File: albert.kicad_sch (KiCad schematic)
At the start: 0 parts

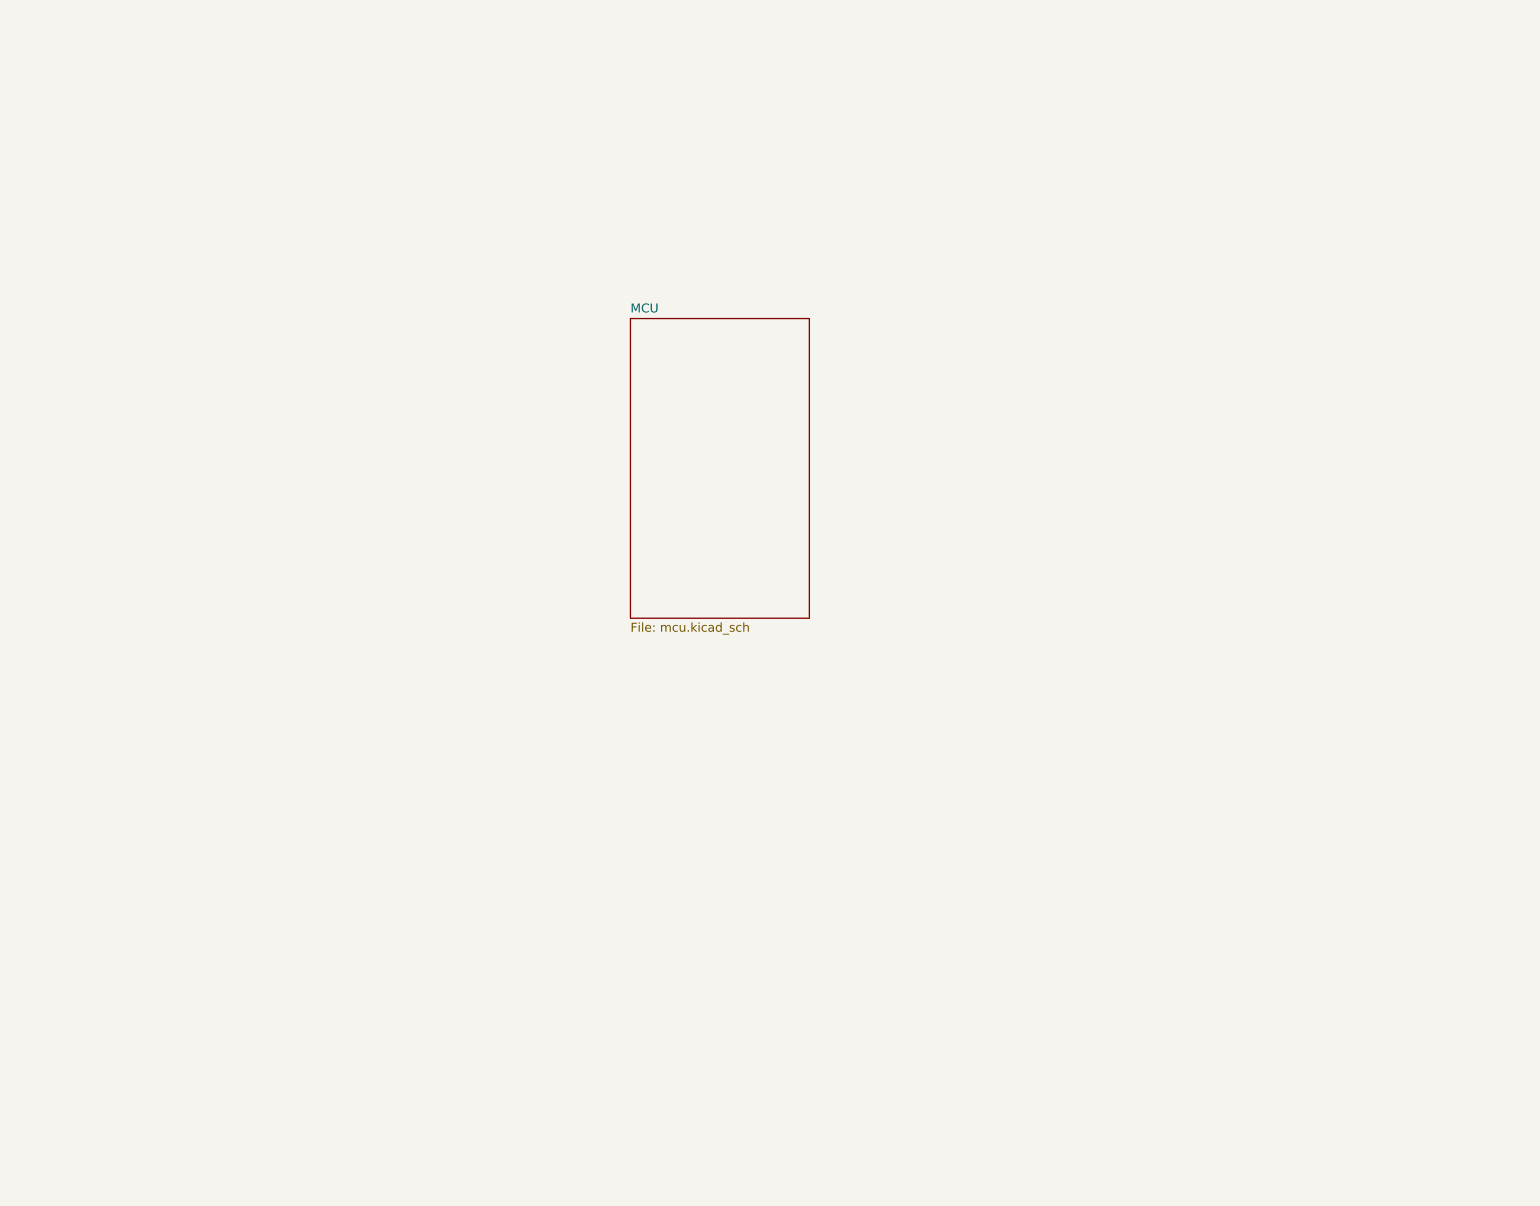
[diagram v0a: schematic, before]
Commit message: Finished XMOS schematic, began work on board connectors
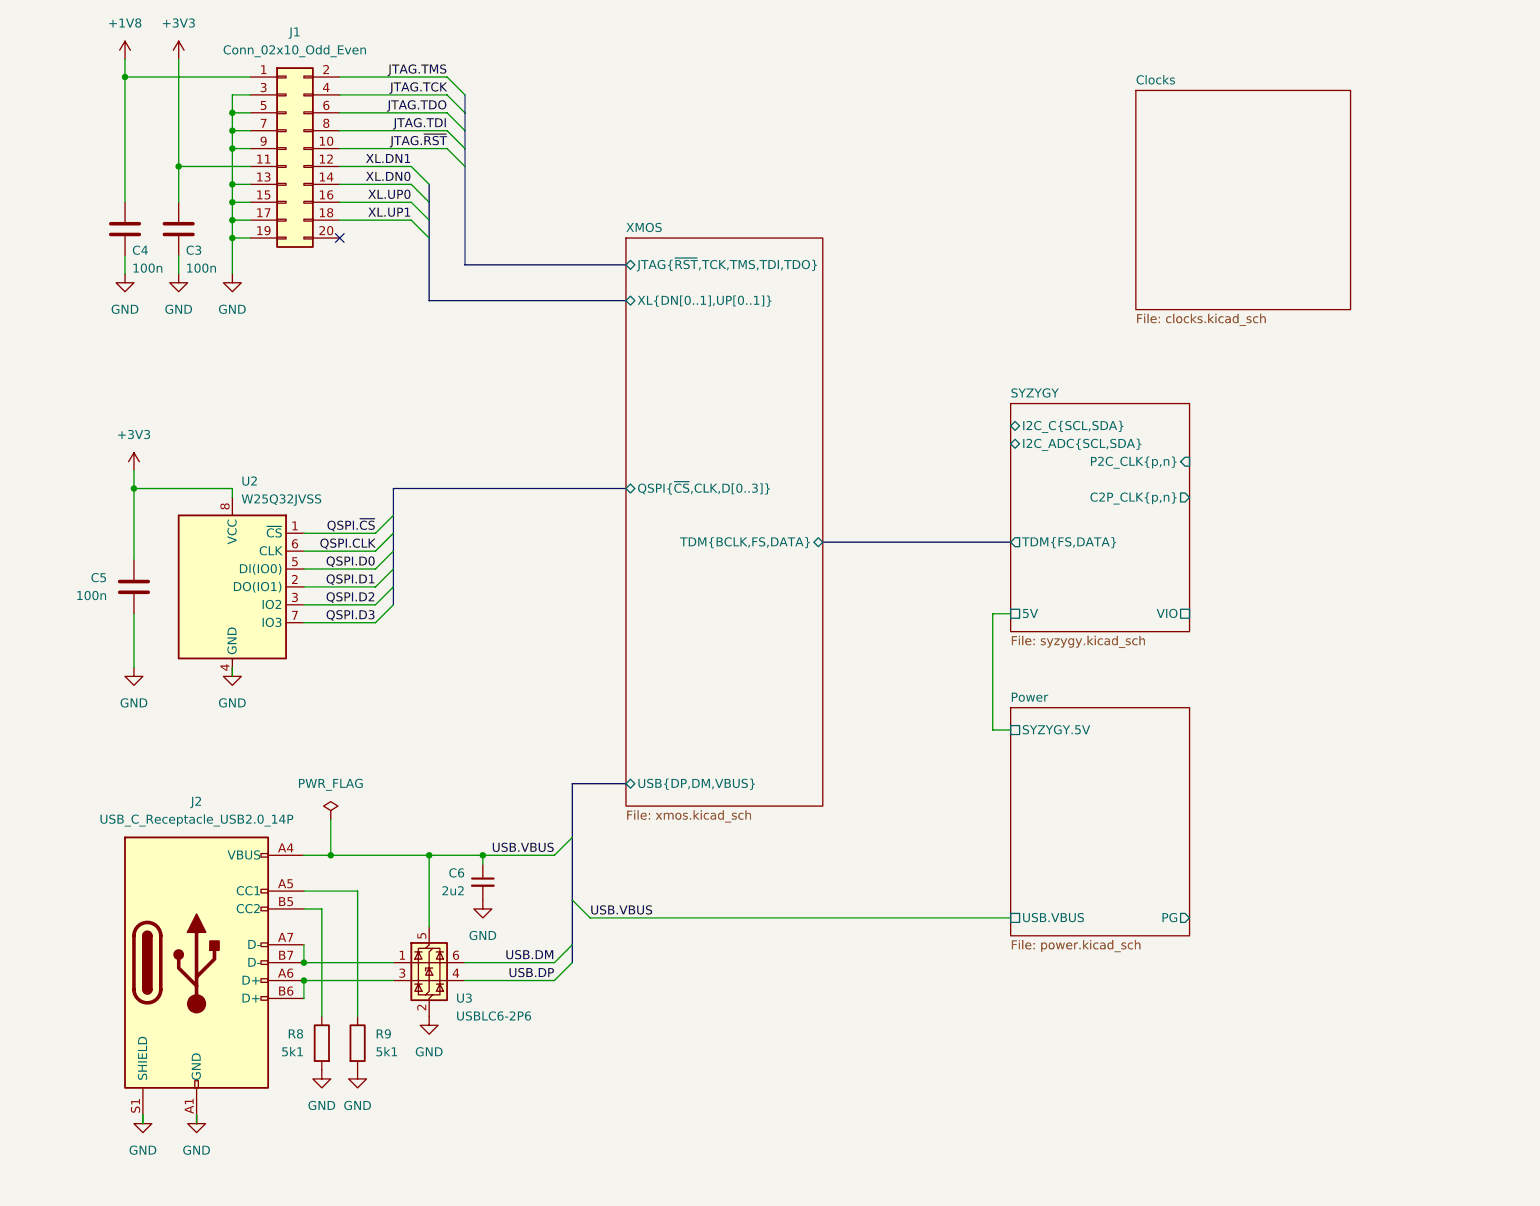
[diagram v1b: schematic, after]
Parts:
- added C3, C4, C5: 100n, symbol Device:C
- added C6: 2u2, symbol Device:C_Small
- added J1: Conn_02x10_Odd_Even, symbol Connector_Generic:Conn_02x10_Odd_Even
- added J2: USB_C_Receptacle_USB2.0_14P, symbol Connector:USB_C_Receptacle_USB2.0_14P
- added R8, R9: 5k1, symbol Device:R
- added U2: W25Q32JVSS, Package_SO:SOIC-8_5.23x5.23mm_P1.27mm, symbol Memory_Flash:W25Q32JVSS
- added U3: USBLC6-2P6, Package_TO_SOT_SMD:SOT-666, symbol Power_Protection:USBLC6-2P6
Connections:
- new net: J2.A7 (D-), J2.B7 (D-), U3.1 (I/O1)
- new net: J2.A6 (D+), J2.B6 (D+), U3.3 (I/O2)
- new net: J2.B5 (CC2), R8.1
- new net: J2.A5 (CC1), R9.1
- new net +1V8: C4.1, J1.1 (Pin_1)
- new net +3V3: C3.1, C5.1, J1.11 (Pin_11), U2.8 (VCC)
- new net GND: C3.2, C4.2, C5.2, C6.2, J1.13 (Pin_13), J1.15 (Pin_15), J1.17 (Pin_17), J1.19 (Pin_19), J1.3 (Pin_3), J1.5 (Pin_5), J1.7 (Pin_7), J1.9 (Pin_9), J2.A1 (GND), J2.A12 (GND), J2.B1 (GND), J2.B12 (GND), J2.S1 (SHIELD), R8.2, R9.2, U2.4 (GND), U3.2 (GND)
- new net JTAG.TCK: J1.4 (Pin_4)
- new net JTAG.TDI: J1.8 (Pin_8)
- new net JTAG.TDO: J1.6 (Pin_6)
- new net JTAG.TMS: J1.2 (Pin_2)
- new net JTAG.~{RST}: J1.10 (Pin_10)
- new net QSPI.CLK: U2.6 (CLK)
- new net QSPI.D0: U2.5 (DI(IO0))
- new net QSPI.D1: U2.2 (DO(IO1))
- new net QSPI.D2: U2.3 (IO2)
- new net QSPI.D3: U2.7 (IO3)
- new net QSPI.~{CS}: U2.1 (~{CS})
- new net USB.DM: U3.6 (I/O1)
- new net USB.DP: U3.4 (I/O2)
- new net USB.VBUS: C6.1, J2.A4 (VBUS), J2.A9 (VBUS), J2.B4 (VBUS), J2.B9 (VBUS), U3.5 (VBUS)
- new net XL.DN0: J1.14 (Pin_14)
- new net XL.DN1: J1.12 (Pin_12)
- new net XL.UP0: J1.16 (Pin_16)
- new net XL.UP1: J1.18 (Pin_18)
- no-connect marks 0 -> 1
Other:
- sheet MCU renamed XMOS
- added sheet Clocks (clocks.kicad_sch)
- added sheet Power (power.kicad_sch)
- added sheet SYZYGY (syzygy.kicad_sch)
- sheet XMOS: file mcu.kicad_sch -> xmos.kicad_sch
- sheet XMOS ports: added JTAG{~{RST},TCK,TMS,TDI,TDO}, QSPI{~{CS},CLK,D[0..3]}, TDM{BCLK,FS,DATA}, USB{DP,DM,VBUS}, XL{DN[0..1],UP[0..1]}; removed none

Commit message: Converted connector power to global labels
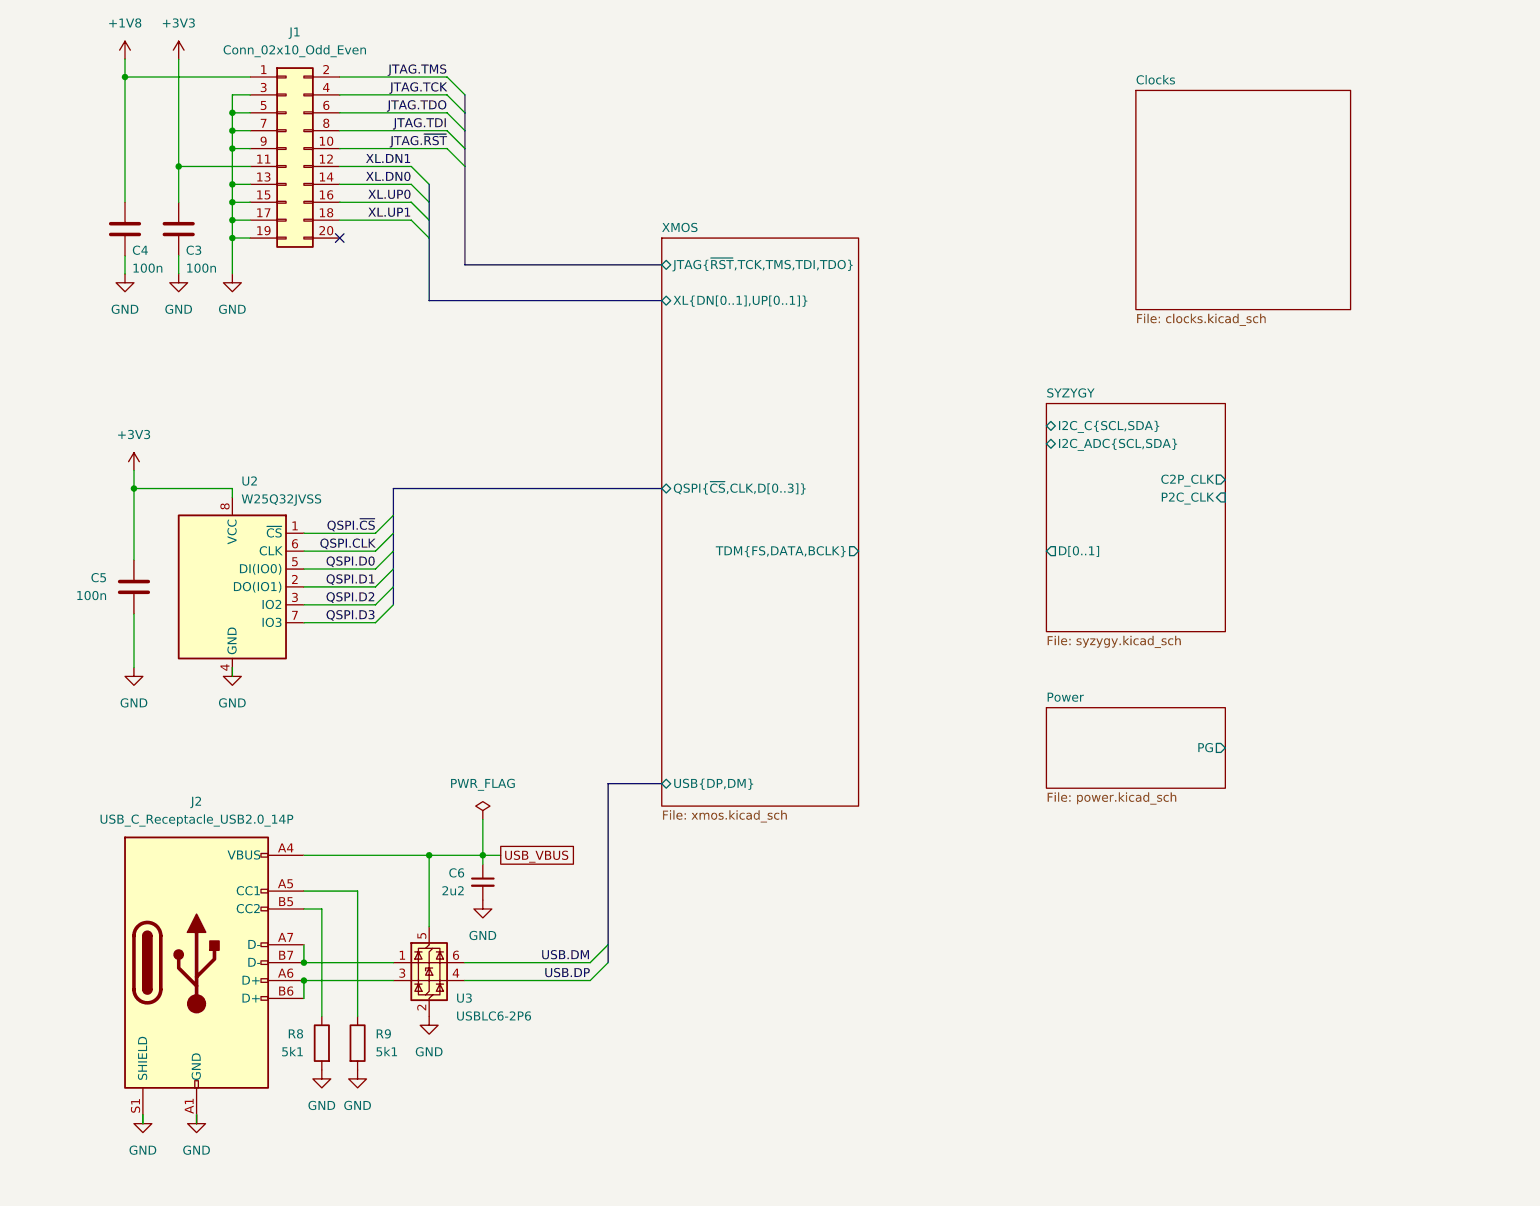
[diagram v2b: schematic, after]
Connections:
- net USB.VBUS renamed USB_VBUS
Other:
- sheet Power ports: added none; removed SYZYGY.5V, USB.VBUS
- sheet SYZYGY ports: added C2P_CLK, D[0..1], P2C_CLK; removed 5V, C2P_CLK{p,n}, P2C_CLK{p,n}, TDM{FS,DATA}, VIO
- sheet XMOS ports: added TDM{FS,DATA,BCLK}, USB{DP,DM}; removed TDM{BCLK,FS,DATA}, USB{DP,DM,VBUS}

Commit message: Minor updates
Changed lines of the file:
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@@
+	)
+	(bus_entry
+		(at 151.13 95.25)
+		(size 2.54 2.54)
+		(stroke
+			(width 0)
+			(type default)
+		)
 	)
 	(bus_entry
@@
 	)
 	(bus_entry
+		(at 148.59 76.2)
+		(size 2.54 2.54)
+		(stroke
+			(width 0)
+			(type default)
+		)
+	)
+	(bus_entry
+		(at 148.59 76.2)
+		(size 2.54 -2.54)
+		(stroke
+			(width 0)
+			(type default)
+		)
+	)
+	(bus_entry
 		(at 74.93 50.8)
+		(size 2.54 2.54)
+		(stroke
+			(width 0)
+			(type default)
+		)
+	)
+	(bus_entry
+		(at 148.59 95.25)
 		(size 2.54 2.54)
 		(stroke
@@
 	)
 	(bus_entry
+		(at 146.05 76.2)
+		(size 2.54 2.54)
+		(stroke
+			(width 0)
+			(type default)
+		)
+	)
+	(bus_entry
 		(at 69.85 97.79)
 		(size 2.54 -2.54)
@@
 		)
 	)
+	(bus
+		(pts
+			(xy 153.67 97.79) (xy 165.1 97.79)
+		)
+		(stroke
+			(width 0)
+			(type default)
+		)
+	)
 	(wire
 		(pts
@@
 		)
 	)
+	(bus
+		(pts
+			(xy 151.13 97.79) (xy 153.67 97.79)
+		)
+		(stroke
+			(width 0)
+			(type default)
+		)
+	)
+	(bus
+		(pts
+			(xy 138.43 76.2) (xy 146.05 76.2)
+		)
+		(stroke
+			(width 0)
+			(type default)
+		)
+	)
+	(bus
+		(pts
+			(xy 146.05 76.2) (xy 148.59 76.2)
+		)
+		(stroke
+			(width 0)
+			(type default)
+		)
+	)
+	(wire
+		(pts
+			(xy 148.59 78.74) (xy 148.59 95.25)
+		)
+		(stroke
+			(width 0)
+			(type default)
+		)
+	)
 	(wire
 		(pts
@@
 		)
 	)
+	(wire
+		(pts
+			(xy 151.13 78.74) (xy 151.13 95.25)
+		)
+		(stroke
+			(width 0)
+			(type default)
+		)
+	)
 	(bus
 		(pts
@@
 		(pts
 			(xy 49.53 115.57) (xy 49.53 114.3)
+		)
+		(stroke
+			(width 0)
+			(type default)
+		)
+	)
+	(wire
+		(pts
+			(xy 151.13 63.5) (xy 151.13 73.66)
 		)
 		(stroke
@@
 		)
 	)
-	(label "QSPI.D2"
-		(at 69.85 105.41 180)
+	(label "D1"
+		(at 148.59 95.25 90)
 		(fields_autoplaced yes)
 		(effects
@@
 				(size 1.27 1.27)
 			)
-			(justify right bottom)
-		)
-	)
-	(label "JTAG.TCK"
-		(at 80.01 33.02 180)
+			(justify left bottom)
+		)
+	)
+	(label "TDM.DATA"
+		(at 151.13 78.74 270)
 		(fields_autoplaced yes)
 		(effects
@@
 		)
 	)
-	(label "XL.UP1"
-		(at 74.93 50.8 180)
+	(label "QSPI.D2"
+		(at 69.85 105.41 180)
 		(fields_autoplaced yes)
 		(effects
@@
 		)
 	)
-	(label "QSPI.~{CS}"
-		(at 69.85 95.25 180)
+	(label "JTAG.TCK"
+		(at 80.01 33.02 180)
 		(fields_autoplaced yes)
 		(effects
@@
 		)
 	)
-	(label "USB.DM"
-		(at 100.33 156.21 180)
+	(label "XL.UP1"
+		(at 74.93 50.8 180)
 		(fields_autoplaced yes)
 		(effects
@@
 		)
 	)
-	(label "QSPI.D3"
-		(at 69.85 107.95 180)
+	(label "QSPI.~{CS}"
+		(at 69.85 95.25 180)
 		(fields_autoplaced yes)
 		(effects
@@
 		)
 	)
-	(label "QSPI.CLK"
-		(at 69.85 97.79 180)
+	(label "USB.DM"
+		(at 100.33 156.21 180)
 		(fields_autoplaced yes)
 		(effects
@@
 		)
 	)
-	(label "JTAG.TMS"
-		(at 80.01 30.48 180)
+	(label "QSPI.D3"
+		(at 69.85 107.95 180)
 		(fields_autoplaced yes)
 		(effects
@@
 		)
 	)
-	(label "JTAG.TDI"
-		(at 80.01 38.1 180)
+	(label "TDM.FS"
+		(at 148.59 78.74 270)
 		(fields_autoplaced yes)
 		(effects
@@
 		)
 	)
-	(label "JTAG.~{RST}"
-		(at 80.01 40.64 180)
+	(label "QSPI.CLK"
+		(at 69.85 97.79 180)
 		(fields_autoplaced yes)
 		(effects
@@
 		)
 	)
-	(label "USB.DP"
-		(at 100.33 158.75 180)
+	(label "JTAG.TMS"
+		(at 80.01 30.48 180)
 		(fields_autoplaced yes)
 		(effects
@@
 			)
 			(justify right bottom)
+		)
+	)
+	(label "D0"
+		(at 151.13 95.25 90)
+		(fields_autoplaced yes)
+		(effects
+			(font
+				(size 1.27 1.27)
+			)
+			(justify left bottom)
+		)
+	)
+	(label "JTAG.TDI"
+		(at 80.01 38.1 180)
+		(fields_autoplaced yes)
+		(effects
+			(font
+				(size 1.27 1.27)
+			)
+			(justify right bottom)
+		)
+	)
+	(label "JTAG.~{RST}"
+		(at 80.01 40.64 180)
+		(fields_autoplaced yes)
+		(effects
+			(font
+				(size 1.27 1.27)
+			)
+			(justify right bottom)
+		)
+	)
+	(label "USB.DP"
+		(at 100.33 158.75 180)
+		(fields_autoplaced yes)
+		(effects
+			(font
+				(size 1.27 1.27)
+			)
+			(justify right bottom)
+		)
+	)
+	(label "TDM.BCLK"
+		(at 151.13 73.66 90)
+		(fields_autoplaced yes)
+		(effects
+			(font
+				(size 1.27 1.27)
+			)
+			(justify left bottom)
 		)
 	)
@@
 		)
 		(pin "TDM{FS,DATA,BCLK}" output
-			(at 138.43 97.79 0)
+			(at 138.43 76.2 0)
 			(effects
 				(font
@@
 	)
 	(sheet
-		(at 177.8 32.385)
-		(size 30.48 31.115)
+		(at 165.1 34.925)
+		(size 25.4 31.115)
 		(fields_autoplaced yes)
 		(stroke
@@
 		)
 		(property "Sheetname" "Clocks"
-			(at 177.8 31.6734 0)
+			(at 165.1 34.2134 0)
 			(effects
 				(font
@@
 		)
 		(property "Sheetfile" "clocks.kicad_sch"
-			(at 177.8 64.0846 0)
-			(effects
-				(font
+			(at 165.1 66.6246 0)
+			(effects
+				(font
